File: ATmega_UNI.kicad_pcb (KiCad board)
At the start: 2 copper layers, 53.3 x 68.6 mm, 42 parts, among them J1 PDIP_1_to_14, J11 PDIP_1_to_14, J13 3.3V, J2 PDIP_15_to_28, J22 PDIP_15_to_28, J5 PWR_Jack, J611 I2C, J612 I2C, J62 4uni, J63 4uni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

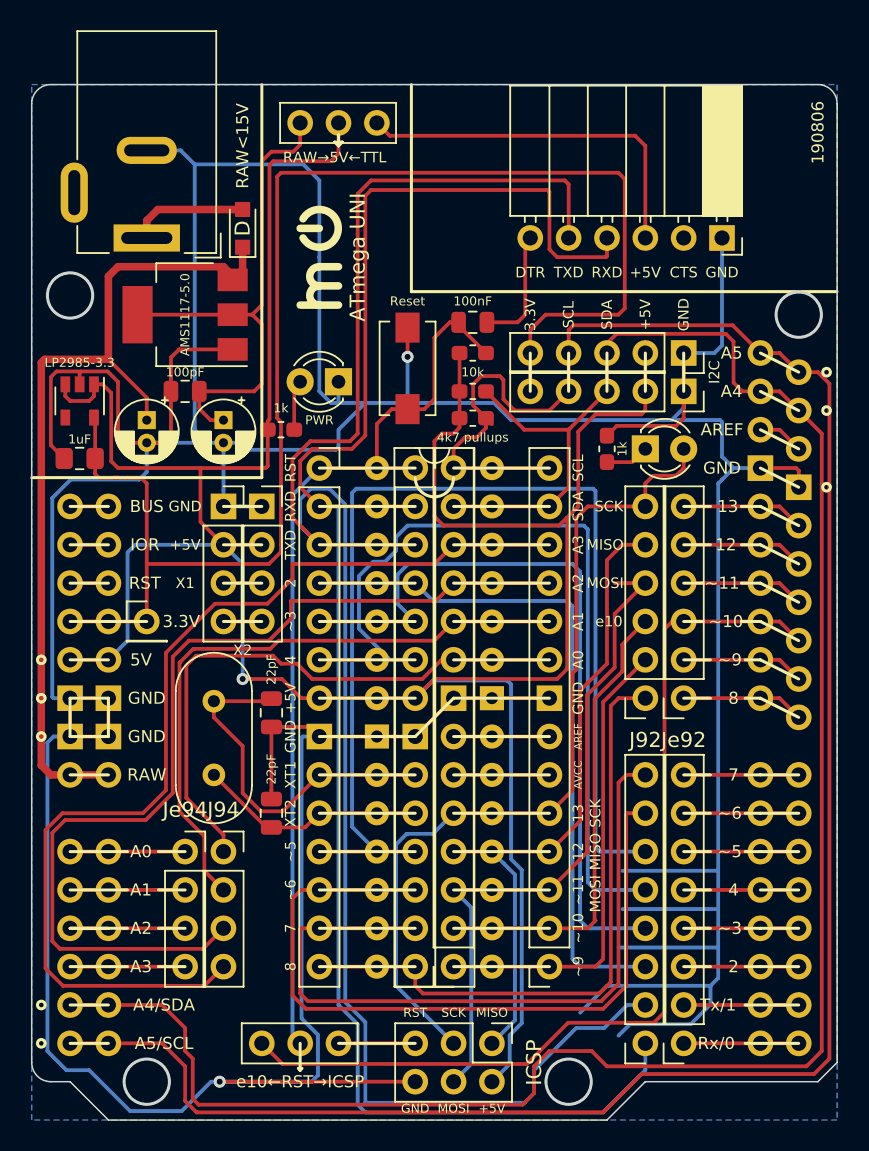
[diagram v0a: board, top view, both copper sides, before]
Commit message: tht push reset button
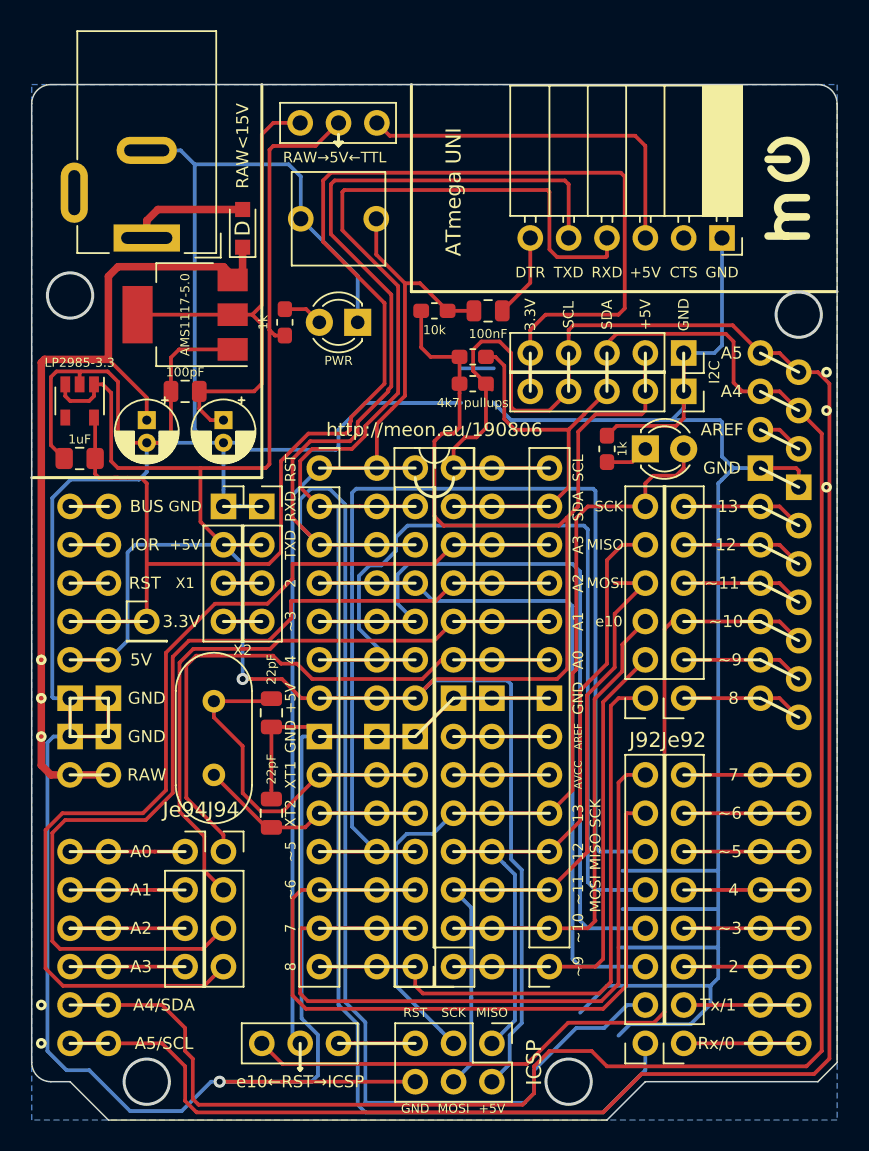
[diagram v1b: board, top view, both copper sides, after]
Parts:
- SW1: footprint Button_Switch_SMD:SW_SPST_EVQPE1 -> Button_Switch_THT:SW_PUSH_6.2mm_DTST_6
- U1: footprint Package_DIP:DIP-28_W7.62mm -> Package_DIP:DIP-28_W7.62mm_big_holes
- moved REF** 31.3 mm to (116.1, 52.6)
- moved SW1 10.9 mm to (86.4, 54.6), turned to 180 degrees
- moved R9 7.12 mm to (82.8, 61.5), turned to 270 degrees
- moved D9 4.14 mm to (87.6, 61.5)
- moved R2 3.78 mm to (92.7, 60.7)
- moved R1 2.29 mm to (95.2, 63.8)
- moved R3 2.29 mm to (95.2, 65.5)
- moved C2 1.27 mm to (96.3, 60.7)
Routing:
- net GND: track 373.7 -> 359.8 mm, vias 2 -> 1
- net ~RST: track 61.7 -> 68.7 mm
- net +5V: track 185.2 -> 190.7 mm
- net TXD: track 121.2 -> 125.9 mm
- net SCL: track 145.7 -> 150.3 mm
- net RXD: track 115.8 -> 119.9 mm
- net SDA: track 143.3 -> 146.3 mm
- net +3V3: track 99.1 -> 101.7 mm
- net DTR: track 7.97 -> 5.59 mm
- net Net-(D9-Pad2): track 3.34 -> 2.65 mm
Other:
- board text removed: "190806"

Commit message: switch female/male connectors, add more SilkS lines
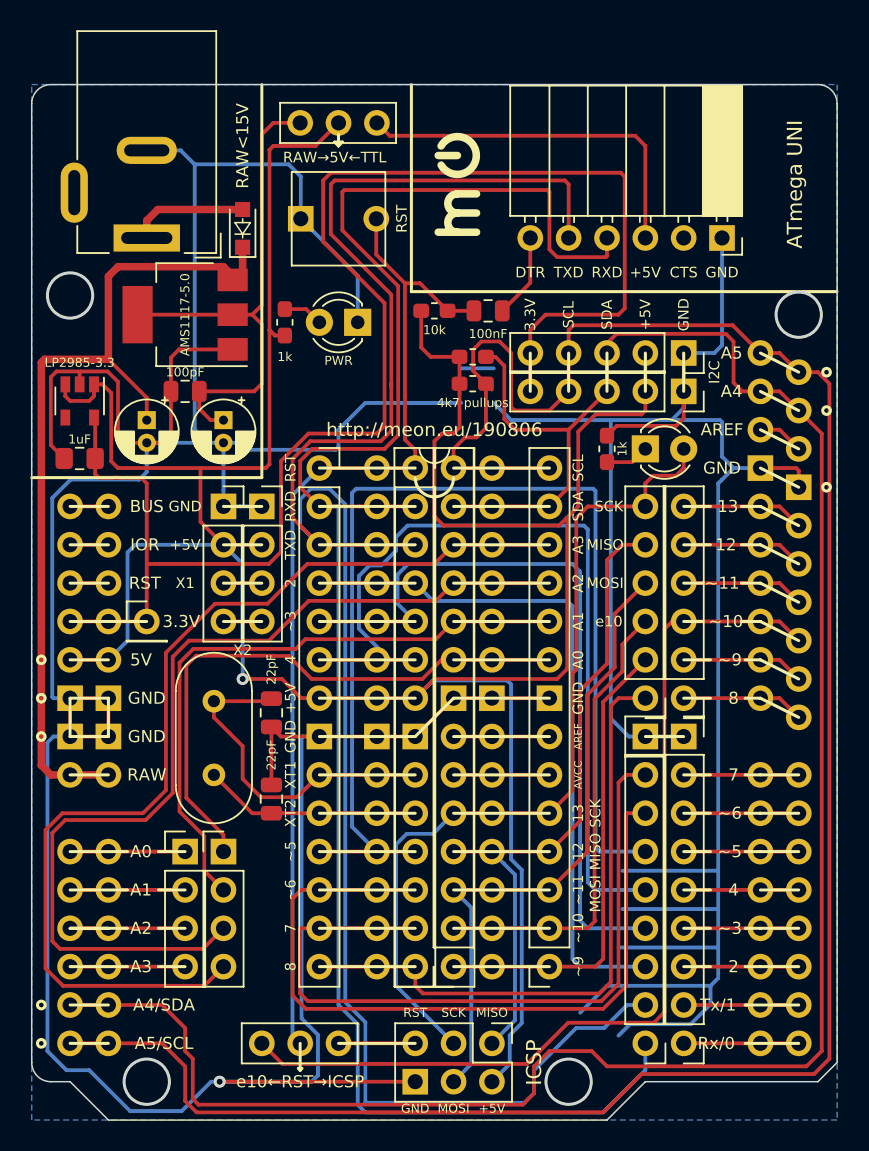
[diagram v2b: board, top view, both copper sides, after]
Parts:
- added J99: extra_gnd, Connector_PinHeader_2.54mm:PinHeader_1x02_P2.54mm_Vertical, F.Cu at (109.2, 88.9)
- D5: footprint Diode_SMD:D_SOD-323_HandSoldering -> Diode_SMD:D_SOD-323_HandSoldering_F_SilkS_Sym
- J92, Je92: footprint Connector_PinSocket_2.54mm:PinSocket_1x06_P2.54mm_Vertical -> Connector_PinHeader_2.54mm:PinHeader_1x06_P2.54mm_Vertical
- J93, Je93: footprint Connector_PinSocket_2.54mm:PinSocket_1x08_P2.54mm_Vertical -> Connector_PinHeader_2.54mm:PinHeader_1x08_P2.54mm_Vertical
- J94, Je94: footprint Connector_PinSocket_2.54mm:PinSocket_1x04_P2.54mm_Vertical -> Connector_PinHeader_2.54mm:PinHeader_1x04_P2.54mm_Vertical
- moved REF** 21.8 mm to (94.2, 52.3)
- moved C12 0.94 mm to (81.9, 93.0)
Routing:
- net GND: track 359.8 -> 384.0 mm
- net MOSI: track 45.1 -> 43.1 mm
- net TXD: track 125.9 -> 127.3 mm
- net XTAL1: track 23.7 -> 22.4 mm
- net RXD: track 119.9 -> 121.2 mm
- net +3V3: track 101.7 -> 102.9 mm
- net XTAL2: track 15.2 -> 14.4 mm
- net PDIP25: track 65.0 -> 64.3 mm
- net PDIP26: track 69.1 -> 68.5 mm

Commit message: use smd led for power, move away i2c pull-up resistors and around to make space for zif socket
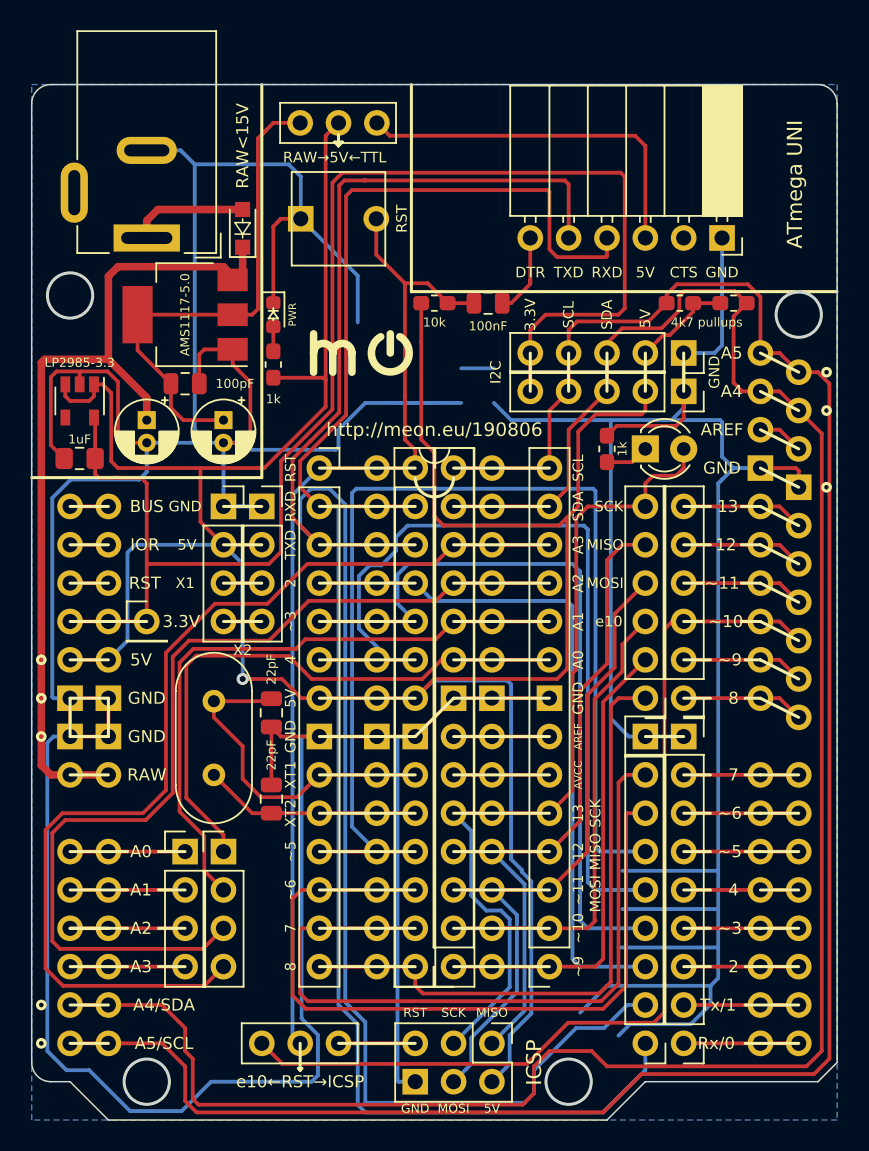
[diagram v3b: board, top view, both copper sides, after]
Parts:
- D9: footprint LED_THT:LED_D3.0mm -> LED_SMD.debian:LED_0603_1608Metric_symbol
- moved R1 17.6 mm to (112.5, 60.2)
- moved R3 14.7 mm to (109.0, 60.2), turned to 0 degrees
- moved REF** 12.9 mm to (87.9, 63.5), turned to 0 degrees
- moved D9 5.61 mm to (82.0, 61.0), turned to 270 degrees
- moved R9 2.90 mm to (82.0, 64.3)
- moved C53 0.51 mm to (76.2, 65.5), turned to 180 degrees
- moved C2 0.51 mm to (96.3, 60.2)
- moved R2 0.51 mm to (92.7, 60.2)
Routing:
- net GND: track 384.0 -> 404.4 mm, vias 1 -> 0
- net SCL: track 150.3 -> 139.5 mm
- net TXD: track 127.3 -> 120.8 mm
- net +3V3: track 102.9 -> 96.4 mm
- net RXD: track 121.2 -> 115.0 mm
- net +5V: track 190.7 -> 196.3 mm
- net SDA: track 146.3 -> 142.4 mm
- net MOSI: track 43.1 -> 44.5 mm
- net Net-(D9-Pad2): track 2.65 -> 1.64 mm
- net Jack_5V: track 34.9 -> 33.9 mm
- net MISO: track 44.2 -> 44.7 mm
- net SCK: track 56.7 -> 56.2 mm
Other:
- board text added: "5V"
- board text removed: "+5V"

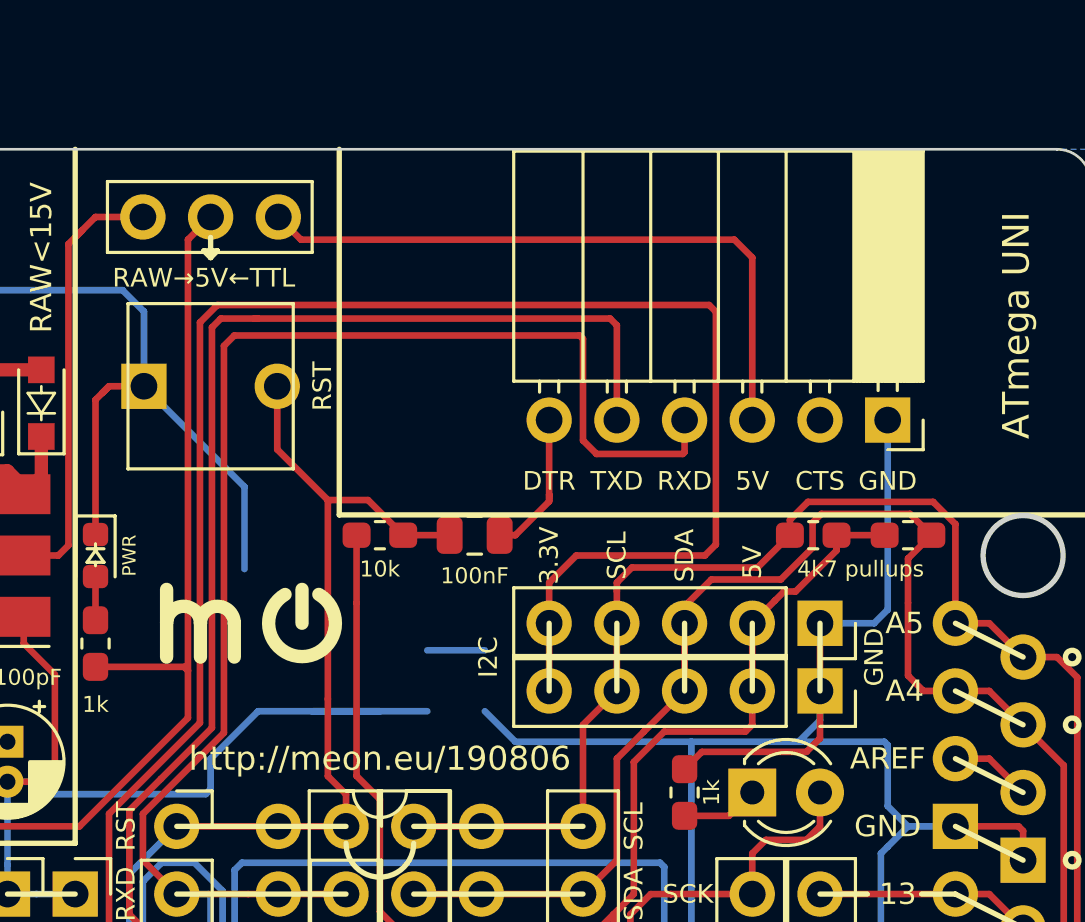
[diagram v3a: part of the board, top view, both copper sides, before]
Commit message: add cp2102 mounting pin
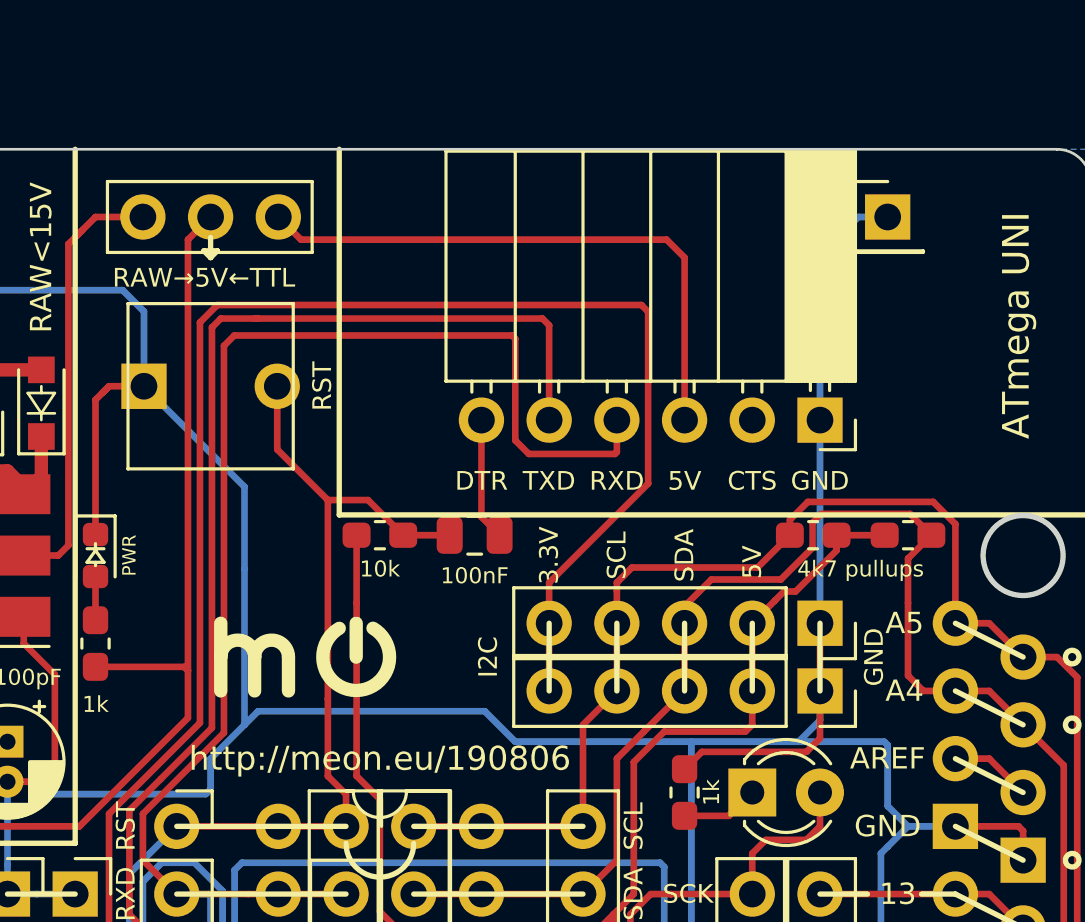
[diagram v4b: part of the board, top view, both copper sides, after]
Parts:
- added J79: GND, Connector_PinHeader_2.54mm:PinHeader_1x01_P2.54mm_Vertical, F.Cu at (111.8, 48.3)
- moved J7 2.54 mm to (109.2, 55.9)
- moved REF** 2.40 mm to (89.9, 64.8)
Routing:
- net GND: track 404.4 -> 414.8 mm
- net +3V3: track 96.4 -> 90.0 mm
- net USB_5V: track 24.5 -> 22.0 mm
- net TXD: track 120.8 -> 118.3 mm
- net RXD: track 115.0 -> 112.5 mm
- net DTR: track 5.61 -> 4.60 mm

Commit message: bump-up the version
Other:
- board text added: "http://meon.eu/190923"
- board text removed: "http://meon.eu/190806"
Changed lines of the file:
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@@
   (gr_line (start 106.68 88.9) (end 109.22 88.9) (layer B.SilkS) (width 0.2))
   (gr_line (start 106.68 88.9) (end 109.22 88.9) (layer F.SilkS) (width 0.2))
-  (gr_text http://meon.eu/190806 (at 92.71 68.58) (layer F.SilkS)
+  (gr_text http://meon.eu/190923 (at 92.71 68.58) (layer F.SilkS)
     (effects (font (size 0.9 0.9) (thickness 0.15)))
   )
@@
     (effects (font (size 0.7 0.7) (thickness 0.15)))
   )
-  (gr_text http://meon.eu/190806 (at 92.71 68.58) (layer B.SilkS)
+  (gr_text http://meon.eu/190923 (at 92.71 68.58) (layer B.SilkS)
     (effects (font (size 0.9 0.9) (thickness 0.15)) (justify mirror))
   )

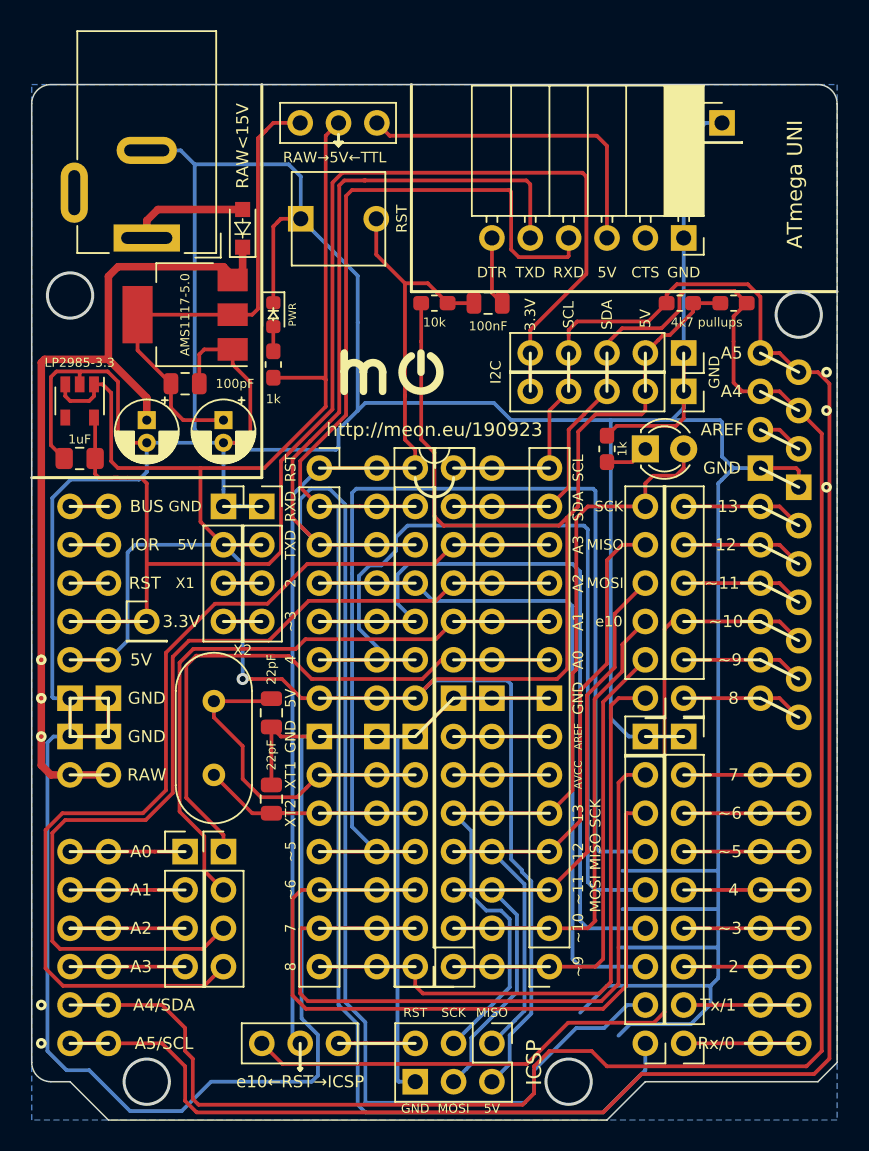
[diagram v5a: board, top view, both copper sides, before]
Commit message: rotate sck led, oval holes, connected pins with SilkS symbols, fix power src text on back
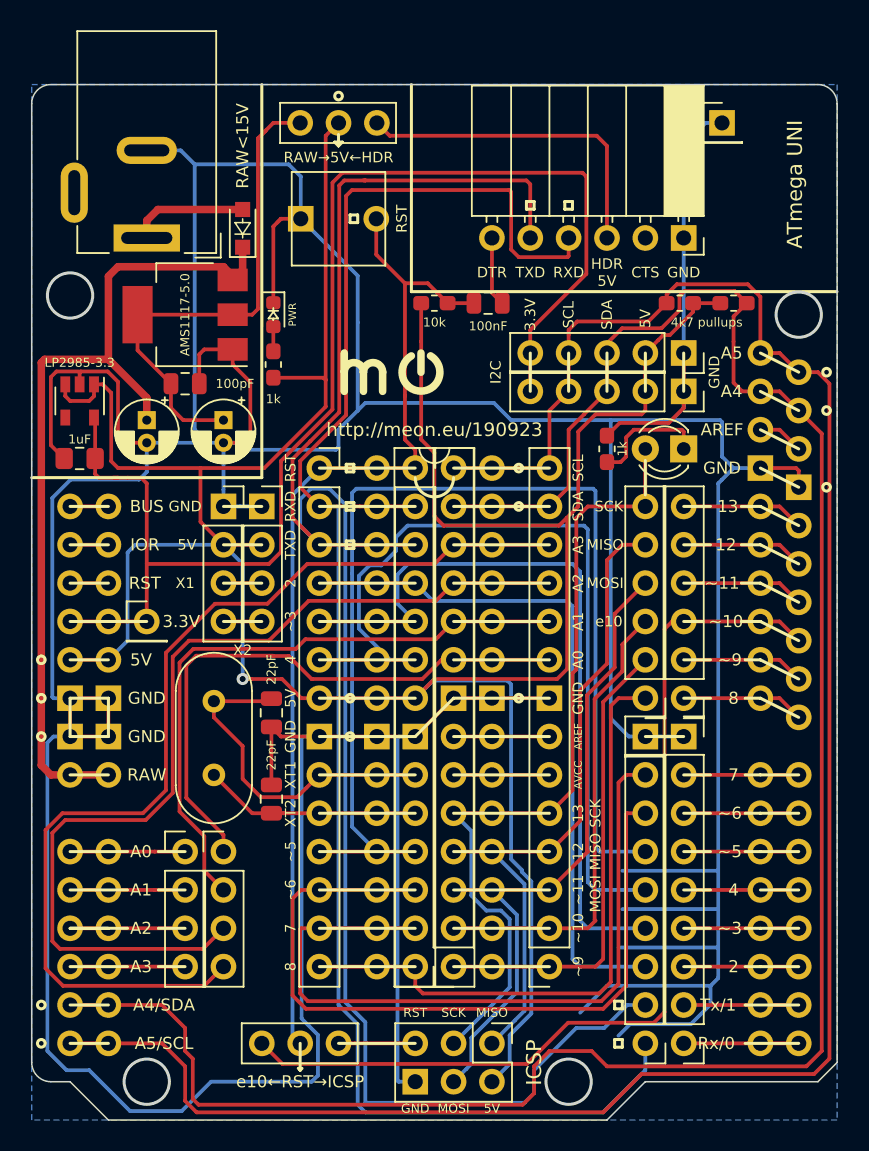
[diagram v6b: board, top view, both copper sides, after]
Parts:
- moved D1 2.54 mm to (109.2, 69.8), turned to 180 degrees
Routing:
- net Net-(D1-Pad1): track 2.90 -> 7.91 mm
- net SCK: track 56.2 -> 54.2 mm
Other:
- board text added: "HDR 5V"
- board text added: "HDR→5V←RAW"
- board text added: "RAW→5V←HDR"
- board text removed: "RAW→5V←TTL"
